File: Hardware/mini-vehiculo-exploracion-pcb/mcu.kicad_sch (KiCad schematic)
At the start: 20 parts, among them J3 UJ20-C-H-G-SMT-5-P16-TR

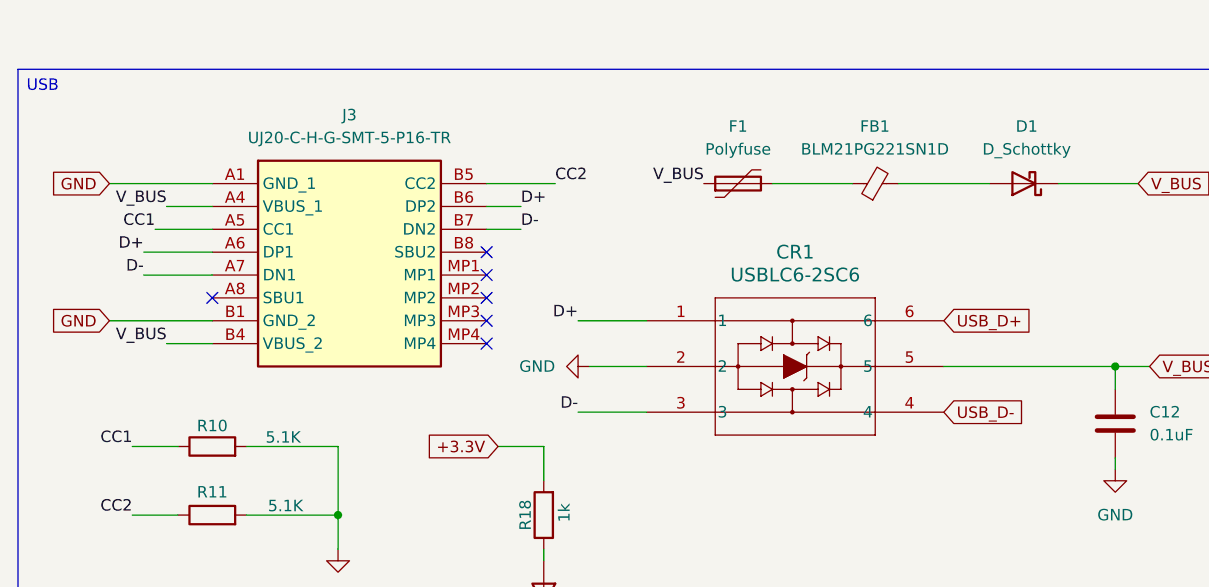
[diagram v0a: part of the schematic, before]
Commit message: Add hardware to main
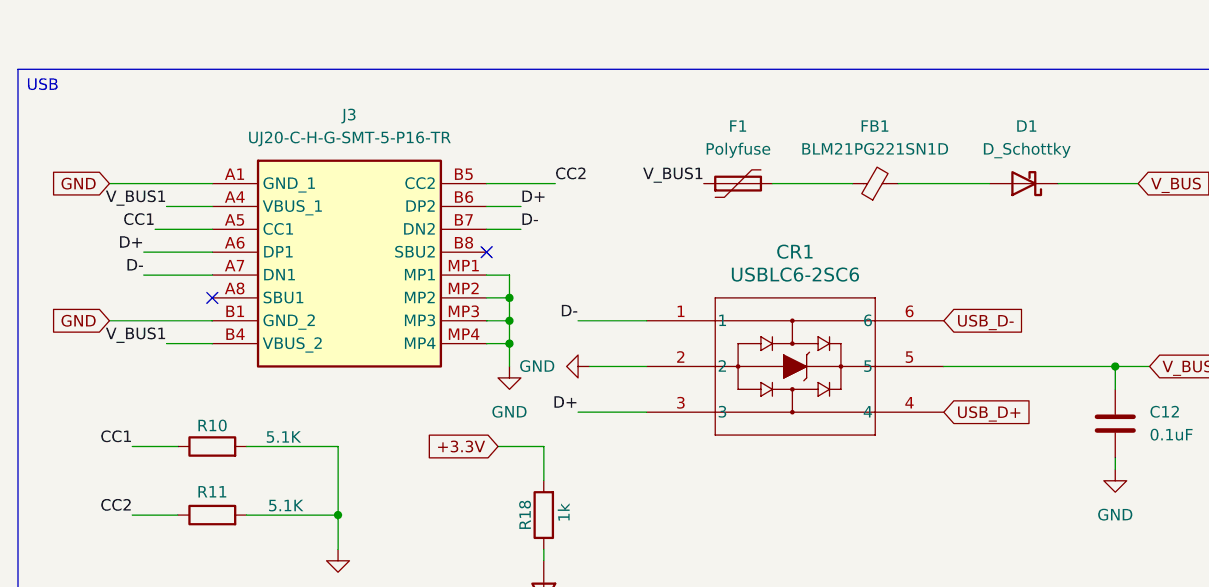
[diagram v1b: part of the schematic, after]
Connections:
- net D+: now also CR1.3; no longer CR1.1
- net D-: now also CR1.1; no longer CR1.3
- net GND: now also J3.MP1, J3.MP2, J3.MP3, J3.MP4
- net USB_D+: now also CR1.4; no longer CR1.6
- net USB_D-: now also CR1.6; no longer CR1.4
- net V_BUS: no longer F1.1, J3.A4 (VBUS_1), J3.B4 (VBUS_2)
- new net V_BUS1: F1.1, J3.A4 (VBUS_1), J3.B4 (VBUS_2)
- no-connect marks 10 -> 6
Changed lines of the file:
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@@
 	)
 	(junction
+		(at 69.85 110.49)
+		(diameter 0)
+		(color 0 0 0 0)
+	)
+	(junction
+		(at 69.85 113.03)
+		(diameter 0)
+		(color 0 0 0 0)
+	)
+	(junction
 		(at 77.47 33.02)
 		(diameter 0)
@@
 	)
 	(junction
+		(at 69.85 115.57)
+		(diameter 0)
+		(color 0 0 0 0)
+	)
+	(junction
 		(at 101.6 48.26)
 		(diameter 0)
@@
 	)
 	(no_connect
-		(at 67.31 110.49)
-	)
-	(no_connect
-		(at 67.31 115.57)
-	)
-	(no_connect
-		(at 67.31 113.03)
-	)
-	(no_connect
-		(at 67.31 107.95)
-	)
-	(no_connect
 		(at 71.12 55.88)
 	)
@@
 	(wire
 		(pts
+			(xy 69.85 110.49) (xy 69.85 113.03)
+		)
+		(stroke
+			(width 0)
+			(type default)
+		)
+	)
+	(wire
+		(pts
 			(xy 73.66 147.32) (xy 73.66 151.13)
 		)
@@
 	(wire
 		(pts
+			(xy 67.31 107.95) (xy 69.85 107.95)
+		)
+		(stroke
+			(width 0)
+			(type default)
+		)
+	)
+	(wire
+		(pts
 			(xy 67.31 102.87) (xy 71.12 102.87)
 		)
@@
 	(wire
 		(pts
+			(xy 69.85 107.95) (xy 69.85 110.49)
+		)
+		(stroke
+			(width 0)
+			(type default)
+		)
+	)
+	(wire
+		(pts
 			(xy 130.81 97.79) (xy 139.7 97.79)
 		)
@@
 	(wire
 		(pts
+			(xy 69.85 113.03) (xy 69.85 115.57)
+		)
+		(stroke
+			(width 0)
+			(type default)
+		)
+	)
+	(wire
+		(pts
 			(xy 101.6 62.23) (xy 104.14 62.23)
 		)
@@
 	(wire
 		(pts
+			(xy 69.85 115.57) (xy 69.85 118.11)
+		)
+		(stroke
+			(width 0)
+			(type default)
+		)
+	)
+	(wire
+		(pts
 			(xy 73.66 130.81) (xy 73.66 127)
 		)
@@
 	(wire
 		(pts
+			(xy 67.31 113.03) (xy 69.85 113.03)
+		)
+		(stroke
+			(width 0)
+			(type default)
+		)
+	)
+	(wire
+		(pts
 			(xy 137.16 118.11) (xy 137.16 120.65)
 		)
@@
 	(wire
 		(pts
+			(xy 67.31 110.49) (xy 69.85 110.49)
+		)
+		(stroke
+			(width 0)
+			(type default)
+		)
+	)
+	(wire
+		(pts
 			(xy 101.6 33.02) (xy 107.95 33.02)
 		)
@@
 	(wire
 		(pts
+			(xy 67.31 115.57) (xy 69.85 115.57)
+		)
+		(stroke
+			(width 0)
+			(type default)
+		)
+	)
+	(wire
+		(pts
 			(xy 77.47 113.03) (xy 85.09 113.03)
 		)
@@
 		)
 	)
-	(label "D-"
+	(label "D+"
 		(at 77.47 123.19 180)
 		(effects
@@
 		)
 	)
-	(label "V_BUS"
+	(label "V_BUS1"
 		(at 31.75 115.57 180)
 		(effects
@@
 		)
 	)
-	(label "V_BUS"
+	(label "V_BUS1"
 		(at 31.75 100.33 180)
 		(effects
@@
 		)
 	)
-	(label "V_BUS"
+	(label "V_BUS1"
 		(at 91.44 97.79 180)
 		(effects
@@
 		)
 	)
-	(label "D+"
+	(label "D-"
 		(at 77.47 113.03 180)
 		(effects
@@
 		)
 	)
-	(global_label "USB_D-"
+	(global_label "USB_D+"
 		(shape input)
 		(at 118.11 123.19 0)
@@
 		)
 	)
-	(global_label "USB_D+"
+	(global_label "USB_D-"
 		(shape input)
 		(at 118.11 113.03 0)
@@
 					(unit 1)
 				)
+			)
+		)
+	)
+	(symbol
+		(lib_id "power:GND")
+		(at 69.85 118.11 0)
+		(unit 1)
+		(exclude_from_sim no)
+		(in_bom yes)
+		(on_board yes)
+		(dnp no)
+		(fields_autoplaced yes)
+		(property "Reference" "#PWR013"
+			(at 69.85 124.46 0)
+			(effects
+				(font
+					(size 1.27 1.27)
+				)
+				(hide yes)
+			)
+		)
+		(property "Value" "GND"
+			(at 69.85 123.19 0)
+			(effects
+				(font
+					(size 1.27 1.27)
+				)
+			)
+		)
+		(property "Footprint" ""
+			(at 69.85 118.11 0)
+			(effects
+				(font
+					(size 1.27 1.27)
+				)
+				(hide yes)
+			)
+		)
+		(property "Datasheet" ""
+			(at 69.85 118.11 0)
+			(effects
+				(font
+					(size 1.27 1.27)
+				)
+				(hide yes)
+			)
+		)
+		(property "Description" "Power symbol creates a global label with name \"GND\" , ground"
+			(at 69.85 118.11 0)
+			(effects
+				(font
+					(size 1.27 1.27)
+				)
+				(hide yes)
+			)
+		)
+		(pin "1"
+		)
+		(instances
+			(project ""
+				(path "/3cb3b833-c38f-47b4-b7e9-f0e6337b7613/7b198334-65f4-4536-9697-14ad78bccec0"
+					(reference "#PWR013")
+					(unit 1)
+				)
